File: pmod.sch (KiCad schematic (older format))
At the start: 13 parts, among them J5 PMOD, U10 TXS0108EPW, U9 AP7381-33SA

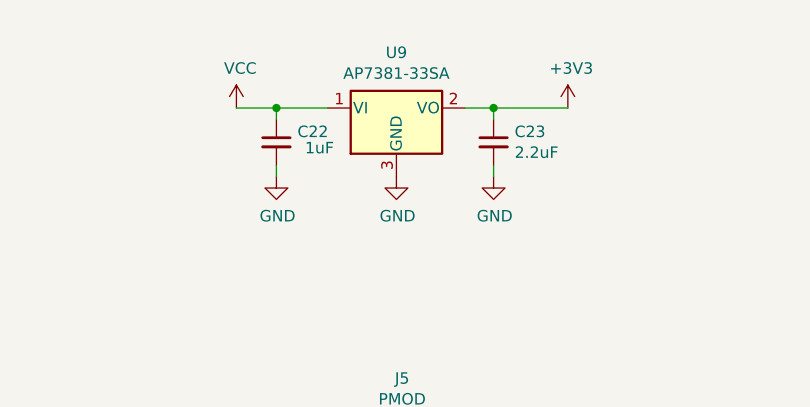
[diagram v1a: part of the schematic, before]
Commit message: changed regulator, routing
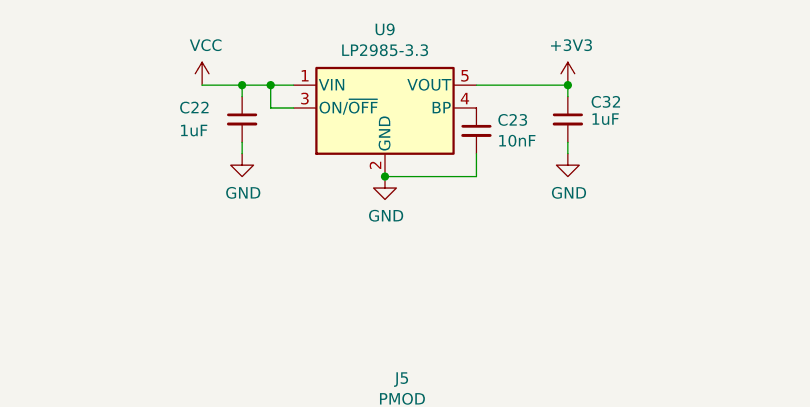
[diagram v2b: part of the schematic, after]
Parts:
- removed U9: AP7381-33SA, Package_TO_SOT_SMD:SOT-23, symbol THS-80-rescue:AP7381-33SA-Regulator_Linear
- added C32: 1uF, Capacitor_SMD:C_0603_1608Metric_Pad1.05x0.95mm_HandSolder, symbol Device:C_Small
- added U9: LP2985-3.3, Package_TO_SOT_SMD:SOT-23-5, symbol Regulator_Linear:LP2985-3.3
- C23: value 2.2uF -> 10nF
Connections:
- wire segments 66 -> 70
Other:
- moved on the sheet: C22, C23
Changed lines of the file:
@@
 L power:+3V3 #PWR?
 U 1 1 5DC93B46
-P 3850 2000
+P 3850 1900
 AR Path="/5D70CA34/5DC93B46" Ref="#PWR?"  Part="1"
 AR Path="/5D70CA34/5DC790D1/5DC93B46" Ref="#PWR047"  Part="1"
-F 0 "#PWR047" H 3850 1850 50  0001 C CNN
-F 1 "+3V3" H 3865 2173 50  0000 C CNN
-F 2 "" H 3850 2000 50  0001 C CNN
-F 3 "" H 3850 2000 50  0001 C CNN
-	1    3850 2000
-	1    0    0    -1
-$EndComp
-Wire Wire Line
-	2575 2000 2400 2000
-Connection ~ 2575 2000
-Wire Wire Line
-	2575 2050 2575 2000
-Wire Wire Line
-	3525 2000 3850 2000
-Connection ~ 3525 2000
-Wire Wire Line
-	3525 2050 3525 2000
-Wire Wire Line
-	3400 2000 3525 2000
-Wire Wire Line
-	2800 2000 2575 2000
-$Comp
-L power:GND #PWR?
-U 1 1 5DC93B54
-P 3100 2300
-AR Path="/5D70CA34/5DC93B54" Ref="#PWR?"  Part="1"
-AR Path="/5D70CA34/5DC790D1/5DC93B54" Ref="#PWR049"  Part="1"
-F 0 "#PWR049" H 3100 2050 50  0001 C CNN
-F 1 "GND" H 3105 2127 50  0000 C CNN
-F 2 "" H 3100 2300 50  0001 C CNN
-F 3 "" H 3100 2300 50  0001 C CNN
-	1    3100 2300
-	1    0    0    -1
-$EndComp
+F 0 "#PWR047" H 3850 1750 50  0001 C CNN
+F 1 "+3V3" H 3865 2073 50  0000 C CNN
+F 2 "" H 3850 1900 50  0001 C CNN
+F 3 "" H 3850 1900 50  0001 C CNN
+	1    3850 1900
+	1    0    0    -1
+$EndComp
+Wire Wire Line
+	2425 1900 2250 1900
+Connection ~ 2425 1900
+Wire Wire Line
+	2425 1950 2425 1900
+Wire Wire Line
+	2650 1900 2550 1900
 $Comp
 L power:GND #PWR?
 U 1 1 5DC93B5A
-P 2575 2300
+P 2425 2200
 AR Path="/5D70CA34/5DC93B5A" Ref="#PWR?"  Part="1"
 AR Path="/5D70CA34/5DC790D1/5DC93B5A" Ref="#PWR048"  Part="1"
-F 0 "#PWR048" H 2575 2050 50  0001 C CNN
-F 1 "GND" H 2580 2127 50  0000 C CNN
-F 2 "" H 2575 2300 50  0001 C CNN
-F 3 "" H 2575 2300 50  0001 C CNN
-	1    2575 2300
-	1    0    0    -1
-$EndComp
-Wire Wire Line
-	2575 2250 2575 2300
+F 0 "#PWR048" H 2425 1950 50  0001 C CNN
+F 1 "GND" H 2430 2027 50  0000 C CNN
+F 2 "" H 2425 2200 50  0001 C CNN
+F 3 "" H 2425 2200 50  0001 C CNN
+	1    2425 2200
+	1    0    0    -1
+$EndComp
+Wire Wire Line
+	2425 2150 2425 2200
 $Comp
 L Device:C_Small C?
 U 1 1 5DC93B61
-P 2575 2150
+P 2425 2050
 AR Path="/5D70CA34/5DC93B61" Ref="C?"  Part="1"
 AR Path="/5D70CA34/5DC790D1/5DC93B61" Ref="C22"  Part="1"
-F 0 "C22" H 2667 2196 50  0000 L CNN
-F 1 "1uF" H 2700 2125 50  0000 L CNN
-F 2 "Capacitor_SMD:C_0603_1608Metric_Pad1.05x0.95mm_HandSolder" H 2575 2150 50  0001 C CNN
-F 3 "~" H 2575 2150 50  0001 C CNN
-	1    2575 2150
+F 0 "C22" H 2150 2100 50  0000 L CNN
+F 1 "1uF" H 2150 2000 50  0000 L CNN
+F 2 "Capacitor_SMD:C_0603_1608Metric_Pad1.05x0.95mm_HandSolder" H 2425 2050 50  0001 C CNN
+F 3 "~" H 2425 2050 50  0001 C CNN
+	1    2425 2050
 	1    0    0    -1
 $EndComp
@@
 L power:GND #PWR?
 U 1 1 5DC93B67
-P 3525 2300
+P 3050 2300
 AR Path="/5D70CA34/5DC93B67" Ref="#PWR?"  Part="1"
 AR Path="/5D70CA34/5DC790D1/5DC93B67" Ref="#PWR050"  Part="1"
-F 0 "#PWR050" H 3525 2050 50  0001 C CNN
-F 1 "GND" H 3530 2127 50  0000 C CNN
-F 2 "" H 3525 2300 50  0001 C CNN
-F 3 "" H 3525 2300 50  0001 C CNN
-	1    3525 2300
-	1    0    0    -1
-$EndComp
-Wire Wire Line
-	3525 2250 3525 2300
+F 0 "#PWR050" H 3050 2050 50  0001 C CNN
+F 1 "GND" H 3055 2127 50  0000 C CNN
+F 2 "" H 3050 2300 50  0001 C CNN
+F 3 "" H 3050 2300 50  0001 C CNN
+	1    3050 2300
+	1    0    0    -1
+$EndComp
 $Comp
 L Device:C_Small C?
 U 1 1 5DC93B6E
-P 3525 2150
+P 3450 2100
 AR Path="/5D70CA34/5DC93B6E" Ref="C?"  Part="1"
 AR Path="/5D70CA34/5DC790D1/5DC93B6E" Ref="C23"  Part="1"
-F 0 "C23" H 3617 2196 50  0000 L CNN
-F 1 "2.2uF" H 3617 2105 50  0000 L CNN
-F 2 "Capacitor_SMD:C_0603_1608Metric_Pad1.05x0.95mm_HandSolder" H 3525 2150 50  0001 C CNN
-F 3 "~" H 3525 2150 50  0001 C CNN
-	1    3525 2150
-	1    0    0    -1
-$EndComp
-$Comp
-L THS-80-rescue:AP7381-33SA-Regulator_Linear U?
-U 1 1 5DC93B74
-P 3100 2000
-AR Path="/5D70CA34/5DC93B74" Ref="U?"  Part="1"
-AR Path="/5D70CA34/5DC790D1/5DC93B74" Ref="U9"  Part="1"
-AR Path="/5DC93B74" Ref="U?"  Part="1"
-F 0 "U9" H 3100 2242 50  0000 C CNN
-F 1 "AP7381-33SA" H 3100 2151 50  0000 C CNN
-F 2 "Package_TO_SOT_SMD:SOT-23" H 3100 2225 50  0001 C CIN
-F 3 "https://www.mouser.com/datasheet/2/115/AP7381-1220674.pdf" H 3100 1950 50  0001 C CNN
-	1    3100 2000
+F 0 "C23" H 3542 2146 50  0000 L CNN
+F 1 "10nF" H 3542 2055 50  0000 L CNN
+F 2 "Capacitor_SMD:C_0603_1608Metric_Pad1.05x0.95mm_HandSolder" H 3450 2100 50  0001 C CNN
+F 3 "~" H 3450 2100 50  0001 C CNN
+	1    3450 2100
 	1    0    0    -1
 $EndComp
@@
 L power:VCC #PWR?
 U 1 1 5DDDFEC8
-P 2400 2000
+P 2250 1900
 AR Path="/5DDDFEC8" Ref="#PWR?"  Part="1"
 AR Path="/5D70CA34/5DC790D1/5DDDFEC8" Ref="#PWR0121"  Part="1"
-F 0 "#PWR0121" H 2400 1850 50  0001 C CNN
-F 1 "VCC" H 2417 2173 50  0000 C CNN
-F 2 "" H 2400 2000 50  0001 C CNN
-F 3 "" H 2400 2000 50  0001 C CNN
-	1    2400 2000
+F 0 "#PWR0121" H 2250 1750 50  0001 C CNN
+F 1 "VCC" H 2267 2073 50  0000 C CNN
+F 2 "" H 2250 1900 50  0001 C CNN
+F 3 "" H 2250 1900 50  0001 C CNN
+	1    2250 1900
 	1    0    0    -1
 $EndComp
@@
 	1    0    0    -1
 $EndComp
+$Comp
+L Regulator_Linear:LP2985-3.3 U9
+U 1 1 5DA3D2AC
+P 3050 2000
+F 0 "U9" H 3050 2342 50  0000 C CNN
+F 1 "LP2985-3.3" H 3050 2251 50  0000 C CNN
+F 2 "Package_TO_SOT_SMD:SOT-23-5" H 3050 2325 50  0001 C CNN
+F 3 "http://www.ti.com/lit/ds/symlink/lp2985.pdf" H 3050 2000 50  0001 C CNN
+	1    3050 2000
+	1    0    0    -1
+$EndComp
+Wire Wire Line
+	2650 2000 2550 2000
+Wire Wire Line
+	2550 2000 2550 1900
+Connection ~ 2550 1900
+Wire Wire Line
+	2550 1900 2425 1900
+Wire Wire Line
+	3450 1900 3850 1900
+Wire Wire Line
+	3050 2300 3450 2300
+Wire Wire Line
+	3450 2300 3450 2200
+Connection ~ 3050 2300
+$Comp
+L power:GND #PWR?
+U 1 1 5DA600E4
+P 3850 2200
+AR Path="/5D70CA34/5DA600E4" Ref="#PWR?"  Part="1"
+AR Path="/5D70CA34/5DC790D1/5DA600E4" Ref="#PWR0138"  Part="1"
+F 0 "#PWR0138" H 3850 1950 50  0001 C CNN
+F 1 "GND" H 3855 2027 50  0000 C CNN
+F 2 "" H 3850 2200 50  0001 C CNN
+F 3 "" H 3850 2200 50  0001 C CNN
+	1    3850 2200
+	1    0    0    -1
+$EndComp
+Wire Wire Line
+	3850 2150 3850 2200
+$Comp
+L Device:C_Small C?
+U 1 1 5DA600EB
+P 3850 2050
+AR Path="/5D70CA34/5DA600EB" Ref="C?"  Part="1"
+AR Path="/5D70CA34/5DC790D1/5DA600EB" Ref="C32"  Part="1"
+F 0 "C32" H 3950 2125 50  0000 L CNN
+F 1 "1uF" H 3950 2050 50  0000 L CNN
+F 2 "Capacitor_SMD:C_0603_1608Metric_Pad1.05x0.95mm_HandSolder" H 3850 2050 50  0001 C CNN
+F 3 "~" H 3850 2050 50  0001 C CNN
+	1    3850 2050
+	1    0    0    -1
+$EndComp
+Wire Wire Line
+	3850 1950 3850 1900
+Connection ~ 3850 1900
 $EndSCHEMATC

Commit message: removed extraneous components
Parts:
- removed D14, D15: SP0504BAHT, Package_TO_SOT_SMD:SOT-23-5, symbol Power_Protection:SP0504BAHT
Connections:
- wire segments 70 -> 62
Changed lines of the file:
@@
 Comment4 ""
 $EndDescr
-Wire Wire Line
-	1925 3800 1925 3400
 $Comp
 L power:+3V3 #PWR?
@@
 $Comp
 L power:GND #PWR?
-U 1 1 5DC93B7A
-P 2025 4200
-AR Path="/5D70CA34/5DC93B7A" Ref="#PWR?"  Part="1"
-AR Path="/5D70CA34/5DC790D1/5DC93B7A" Ref="#PWR060"  Part="1"
-F 0 "#PWR060" H 2025 3950 50  0001 C CNN
-F 1 "GND" H 2030 4027 50  0000 C CNN
-F 2 "" H 2025 4200 50  0001 C CNN
-F 3 "" H 2025 4200 50  0001 C CNN
-	1    2025 4200
-	1    0    0    -1
-$EndComp
-$Comp
-L power:GND #PWR?
-U 1 1 5DC93B80
-P 4075 4200
-AR Path="/5D70CA34/5DC93B80" Ref="#PWR?"  Part="1"
-AR Path="/5D70CA34/5DC790D1/5DC93B80" Ref="#PWR063"  Part="1"
-F 0 "#PWR063" H 4075 3950 50  0001 C CNN
-F 1 "GND" H 4080 4027 50  0000 C CNN
-F 2 "" H 4075 4200 50  0001 C CNN
-F 3 "" H 4075 4200 50  0001 C CNN
-	1    4075 4200
-	1    0    0    -1
-$EndComp
-$Comp
-L power:GND #PWR?
 U 1 1 5DC93B86
 P 2775 4200
@@
 	2875 3800 2675 3800
 Wire Wire Line
-	4275 3800 4275 3400
-Wire Wire Line
-	4175 3800 4175 3500
-Wire Wire Line
-	4075 3800 4075 3600
-Wire Wire Line
-	3975 3800 3975 3700
-Wire Wire Line
-	2225 3700 2875 3700
-Wire Wire Line
-	2225 3800 2225 3700
-Wire Wire Line
-	2125 3600 2875 3600
-Wire Wire Line
-	2125 3800 2125 3600
-Wire Wire Line
-	2025 3500 2875 3500
-Wire Wire Line
-	2025 3800 2025 3500
-Wire Wire Line
-	1925 3400 2875 3400
-$Comp
-L Power_Protection:SP0504BAHT D?
-U 1 1 5DC93BC1
-P 4075 4000
-AR Path="/5D70CA34/5DC93BC1" Ref="D?"  Part="1"
-AR Path="/5D70CA34/5DC790D1/5DC93BC1" Ref="D15"  Part="1"
-F 0 "D15" H 4400 4050 50  0000 L CNN
-F 1 "SP0504BAHT" H 4400 3950 50  0000 L CNN
-F 2 "Package_TO_SOT_SMD:SOT-23-5" H 4375 3950 50  0001 L CNN
-F 3 "http://www.littelfuse.com/~/media/files/littelfuse/technical%20resources/documents/data%20sheets/sp05xxba.pdf" H 4200 4125 50  0001 C CNN
-	1    4075 4000
-	1    0    0    -1
-$EndComp
-$Comp
-L Power_Protection:SP0504BAHT D?
-U 1 1 5DC93BC7
-P 2025 4000
-AR Path="/5D70CA34/5DC93BC7" Ref="D?"  Part="1"
-AR Path="/5D70CA34/5DC790D1/5DC93BC7" Ref="D14"  Part="1"
-F 0 "D14" H 1350 4050 50  0000 L CNN
-F 1 "SP0504BAHT" H 1350 3950 50  0000 L CNN
-F 2 "Package_TO_SOT_SMD:SOT-23-5" H 2325 3950 50  0001 L CNN
-F 3 "http://www.littelfuse.com/~/media/files/littelfuse/technical%20resources/documents/data%20sheets/sp05xxba.pdf" H 2150 4125 50  0001 C CNN
-	1    2025 4000
-	1    0    0    -1
-$EndComp
-Wire Wire Line
-	3375 3700 3975 3700
-Wire Wire Line
 	3375 3600 4075 3600
-Wire Wire Line
-	3375 3500 4175 3500
-Wire Wire Line
-	3375 3400 4275 3400
 Text Label 3575 3700 0    50   ~ 0
 P10
@@
 	3850 1950 3850 1900
 Connection ~ 3850 1900
+Wire Wire Line
+	3375 3700 4075 3700
+Wire Wire Line
+	3375 3500 4075 3500
+Wire Wire Line
+	3375 3400 4075 3400
+Wire Wire Line
+	2175 3400 2875 3400
+Wire Wire Line
+	2175 3500 2875 3500
+Wire Wire Line
+	2175 3600 2875 3600
+Wire Wire Line
+	2175 3700 2875 3700
 $EndSCHEMATC

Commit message: fixed clocks
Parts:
- J4: renamed from J5; footprint Connector_PinSocket_2.54mm:PinSocket_2x06_P2.54mm_Horizontal -> Connector_PinSocket_2.54mm:PinSocket_2x06_P2.54mm_Horizontal_Top_Bottom
- renumbered C22 to C13, C26 to C14, C23 to C15, C27 to C16, C32 to C17, C24 to C18, C25 to C19, R20 to R7, RN3 to RN4, U9 to U4, U10 to U5

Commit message: do over with additional pmod
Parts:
- removed C13, C17: 1uF, Capacitor_SMD:C_0603_1608Metric_Pad1.05x0.95mm_HandSolder, symbol Device:C_Small
- removed C14, C16, C18, C19: 100nF, Capacitor_SMD:C_0603_1608Metric_Pad1.05x0.95mm_HandSolder, symbol Device:C_Small
- removed C15: 10nF, Capacitor_SMD:C_0603_1608Metric_Pad1.05x0.95mm_HandSolder, symbol Device:C_Small
- removed J4: PMOD, Connector_PinSocket_2.54mm:PinSocket_2x06_P2.54mm_Horizontal_Top_Bottom, symbol Connector_Generic:Conn_02x06_Top_Bottom
- removed R7: 1K, Resistor_SMD:R_0603_1608Metric_Pad1.05x0.95mm_HandSolder, symbol Device:R_Small
- removed RN4: 200R, Resistor_SMD:R_Cat16-8, symbol Device:R_Pack08
- removed U4: LP2985-3.3, Package_TO_SOT_SMD:SOT-23-5, symbol Regulator_Linear:LP2985-3.3
- removed U5: TXS0108EPW, Package_SO:TSSOP-20_4.4x6.5mm_P0.65mm, symbol Logic_LevelTranslator:TXS0108EPW
- added C1, C2, C? (x2): 100nF, Capacitor_SMD:C_0603_1608Metric_Pad1.05x0.95mm_HandSolder, symbol Device:C_Small
- added J2, J?: PMOD, max_breakout:PinSocket_2x06_Top_Bottom_P2.54mm_Horizontal, symbol Connector_Generic:Conn_02x06_Top_Bottom
- added JP1, JP?: ena, Connector_PinHeader_2.54mm:PinHeader_1x02_P2.54mm_Vertical, symbol Device:Jumper_NO_Small
- added R1, R?: 1K, Resistor_SMD:R_0603_1608Metric_Pad1.05x0.95mm_HandSolder, symbol Device:R_Small
- added U1, U?: TXS0108EPW, Package_SO:TSSOP-20_4.4x6.5mm_P0.65mm, symbol Logic_LevelTranslator:TXS0108EPW
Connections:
- net labels added: +5V, 3V3, IO1, IO2, IO3, IO4, IO5, IO6, IO7, IO8A, P42, P43, P44, P5, P6
- net labels removed: OE1, P1, P10, P4, P7, P9, PMOD1, PMOD10, PMOD2, PMOD3, PMOD4, PMOD7, PMOD8, PMOD9, VCC
- wire segments 62 -> 78
